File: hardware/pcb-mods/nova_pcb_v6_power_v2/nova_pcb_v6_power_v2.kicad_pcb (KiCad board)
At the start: 4 copper layers, 112 x 90 mm, 55 parts, among them J1 XT60_4S_IN, J12 XT30_JET_12V, J13 XT30_L2_12V, J2 UBEC_5V_AUX, J20 IB_2x06, J3 XT30_Inj, J4 XT30_Inj, J5 XT30_Inj, J6 XT30_Inj, J7 XT30_Inj, J8 ServoBus_TTL, M1 Voltmeter_DC, Q1 IRLB3034PBF, Q2 BSS138_cutoff, Q3 BSS138_estop, Q4 BSS138_jetcut, SW1 Rocker_30A, SW2 Estop_NC_latching, U1 Pololu_D42V110F7_LEG_7V5, U10 INA226, U11 INA226, U2 Pololu_D42V110F12_HIP_12V, U3 Pololu_D24V22F12_L2_12V, U4 Pololu_D42V55F12_JET_12V, U5 Pololu_D42V55F7_ARM_7V5, U8 LM393, U9 INA226

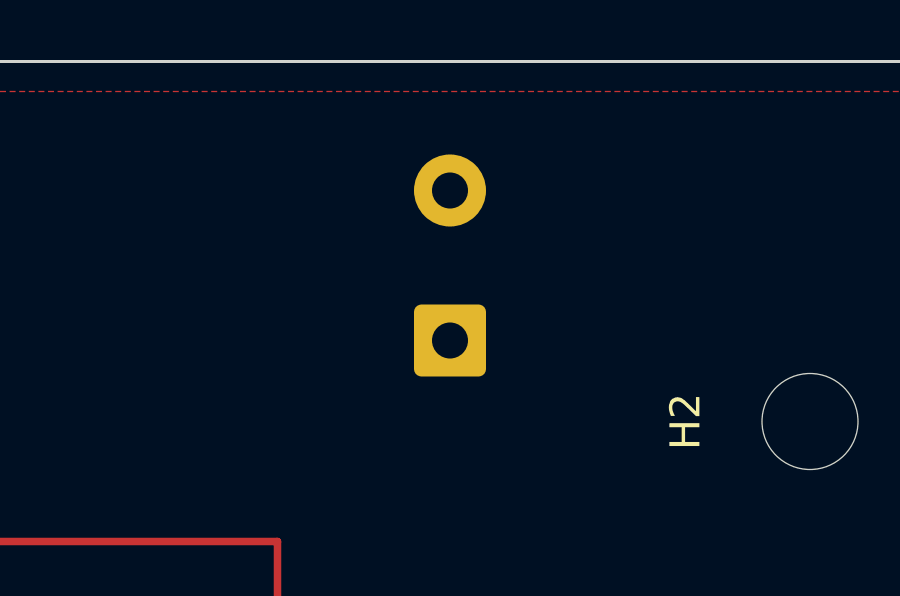
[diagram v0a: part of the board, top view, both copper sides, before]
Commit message: pcb(v6-power-v2): nudge C4 1.0mm inboard — edge clearance 0.3 -> 1.3mm
kicad-happy PM-002 error cleared. Pads feed LEG pour / GND plane only,
no tracks to move. Zones refilled, DRC 0 errors.

Co-Authored-By: Claude Fable 5 <noreply@anthropic.com>
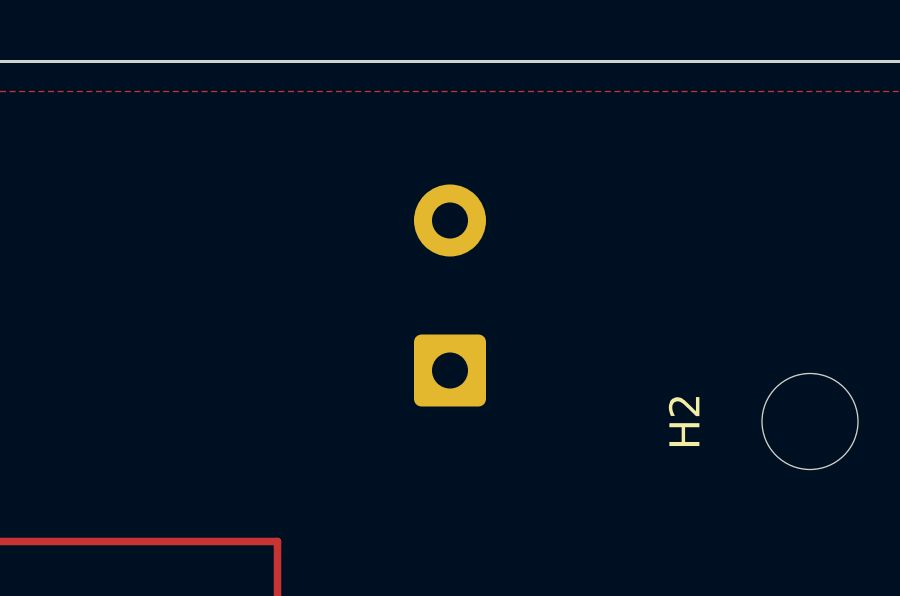
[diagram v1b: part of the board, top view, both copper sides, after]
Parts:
- moved C4 1.00 mm to (165.0, 61.3)
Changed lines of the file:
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@@
 	(footprint "Capacitor_THT:CP_Radial_D12.5mm_P5.00mm"
 		(layer "B.Cu")
-		(at 165 60.3 90)
+		(at 165 61.3 90)
 		(descr "CP, Radial series, Radial, pin pitch=5.00mm, diameter=12.5mm, height=20mm, Electrolytic Capacitor")
 		(tags "CP Radial series Radial pin pitch 5.00mm diameter 12.5mm height 20mm Electrolytic Capacitor")

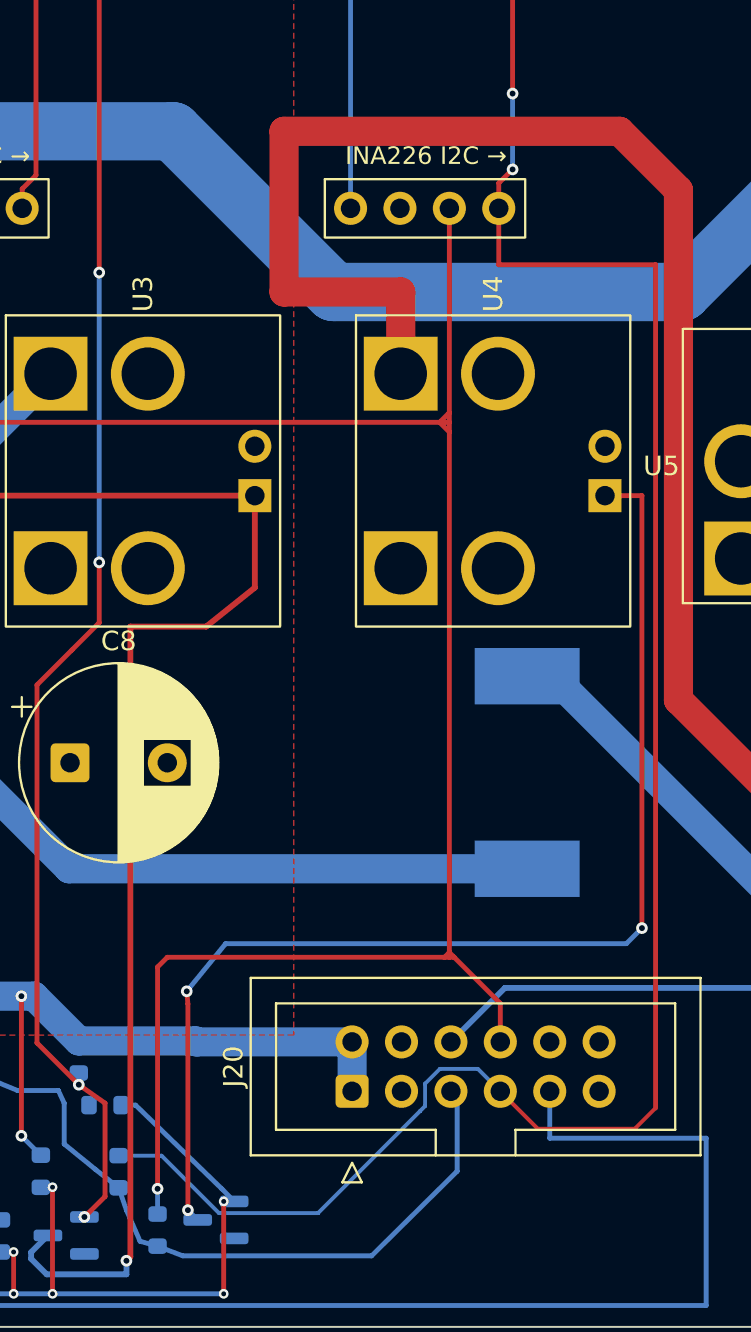
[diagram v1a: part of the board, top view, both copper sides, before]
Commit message: pcb(v6-power-v2): sync nova_v6 library footprints from board — 13->5 DRC mismatch warnings
INA226_Module_Breakout: 12-pad module -> 4-pad I2C header landing
(matches the off-board conversion; descr documents wiring + addresses).
Buck_Offboard_Terminal_2xXT30: synced board geometry to lib.
Remaining 5 warnings (J2 M1 Q1 SW1 SW2) = upstream KiCad 9 stock-lib
drift since placement — cosmetic, deliberately NOT updated pre-fab
(refreshing stock footprints can shift pads under routed copper).
Gerbers never consult libraries; zero fab impact.

Co-Authored-By: Claude Fable 5 <noreply@anthropic.com>
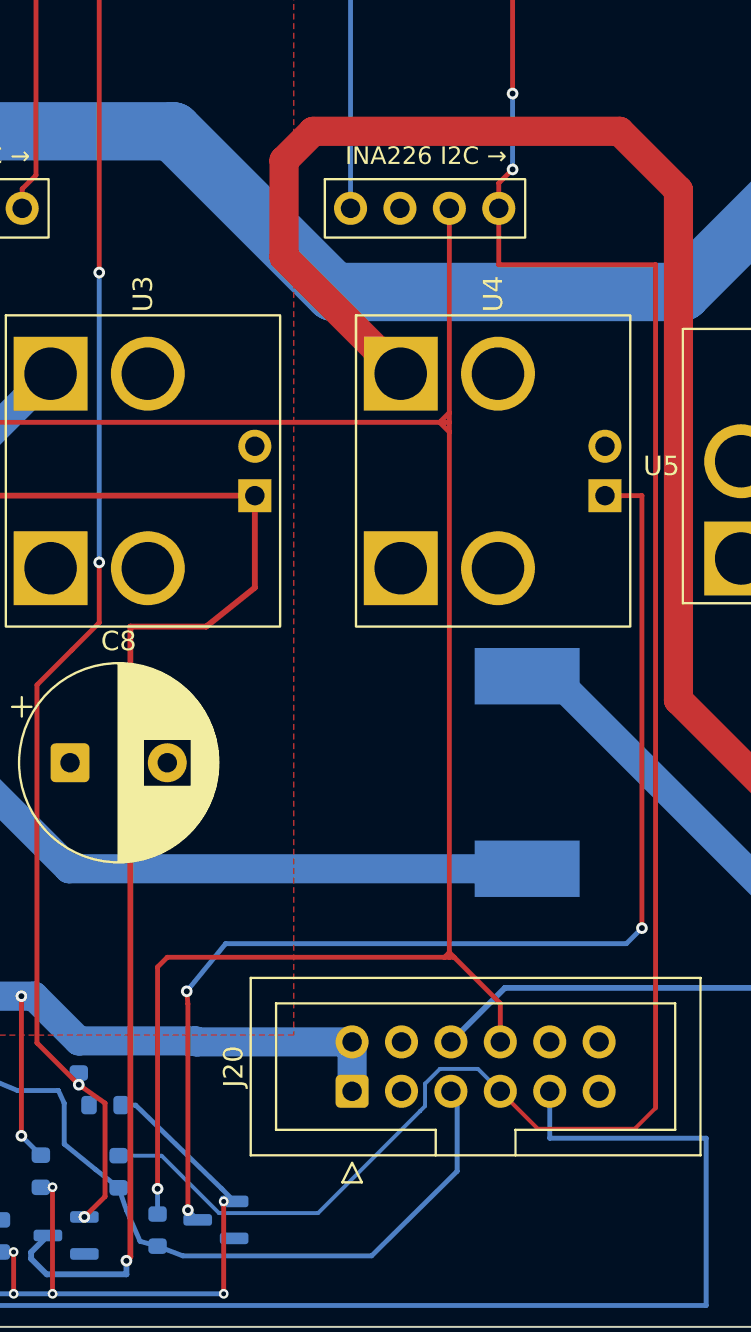
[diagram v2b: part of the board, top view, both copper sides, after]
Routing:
- net V12_JET: track 92.8 -> 88.4 mm
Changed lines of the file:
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@@
 			(pinfunction "Pin_4")
 			(pintype "passive")
+			(teardrops
+				(best_length_ratio 0.5)
+				(max_length 1)
+				(best_width_ratio 1)
+				(max_width 2)
+				(curved_edges no)
+				(filter_ratio 0.9)
+				(enabled yes)
+				(allow_two_segments yes)
+				(prefer_zone_connections yes)
+			)
 		)
 		(embedded_fonts no)
@@
 	)
 	(segment
-		(start 153.5 92)
-		(end 153.5 87.8)
+		(start 147.5 86)
+		(end 147.5 81.04)
 		(width 1.5)
 		(layer "F.Cu")
@@
 	)
 	(segment
-		(start 153.5 87.8)
-		(end 147.5 87.8)
+		(start 153.5 92)
+		(end 147.5 86)
 		(width 1.5)
 		(layer "F.Cu")
@@
 	)
 	(segment
-		(start 147.5 87.8)
-		(end 147.5 79.54)
+		(start 147.5 81.04)
+		(end 149 79.54)
 		(width 1.5)
 		(layer "F.Cu")
@@
 	)
 	(segment
-		(start 147.5 79.54)
+		(start 149 79.54)
 		(end 164.75 79.54)
 		(width 1.5)
@@
 	)
 	(segment
-		(start 111.25 81)
-		(end 110.54 81.8)
-		(width 0.25)
+		(start 139 132.2)
+		(end 141.208032 132.2)
+		(width 0.2)
 		(layer "B.Cu")
 		(net 13)
 	)
 	(segment
-		(start 149.2519 135.151)
-		(end 149.25 135.151)
+		(start 154.75 129.6529)
+		(end 154.75 128.5)
 		(width 0.2)
 		(layer "B.Cu")
@@
 	(segment
 		(start 155.511 127.739)
-		(end 154.75 128.5)
+		(end 157.469 127.739)
 		(width 0.2)
 		(layer "B.Cu")
@@
 	)
 	(segment
-		(start 154.75 128.5)
-		(end 154.75 129.6529)
-		(width 0.2)
+		(start 111.25 81)
+		(end 110.54 81.8)
+		(width 0.25)
 		(layer "B.Cu")
 		(net 13)
 	)
 	(segment
-		(start 158.62 128.89)
-		(end 157.469 127.739)
+		(start 141.208032 132.2)
+		(end 144.159032 135.151)
 		(width 0.2)
 		(layer "B.Cu")
@@
 	)
 	(segment
-		(start 149.25 135.151)
-		(end 144.159032 135.151)
+		(start 154.5 129.9029)
+		(end 154.75 129.6529)
 		(width 0.2)
 		(layer "B.Cu")
@@
 	)
 	(segment
-		(start 157.469 127.739)
-		(end 155.511 127.739)
+		(start 144.159032 135.151)
+		(end 149.25 135.151)
 		(width 0.2)
 		(layer "B.Cu")
@@
 	)
 	(segment
-		(start 154.75 129.6529)
-		(end 154.5 129.9029)
-		(width 0.2)
-		(layer "B.Cu")
-		(net 13)
-	)
-	(segment
-		(start 141.208032 132.2)
-		(end 139 132.2)
+		(start 149.25 135.151)
+		(end 154.4981 129.9029)
 		(width 0.2)
 		(layer "B.Cu")
@@
 	)
 	(segment
-		(start 154.4981 129.9029)
-		(end 149.25 135.151)
+		(start 157.469 127.739)
+		(end 158.62 128.89)
 		(width 0.2)
 		(layer "B.Cu")
@@
 	)
 	(segment
-		(start 144.159032 135.151)
-		(end 141.208032 132.2)
+		(start 154.75 128.5)
+		(end 155.511 127.739)
 		(width 0.2)
 		(layer "B.Cu")
@@
 	)
 	(segment
-		(start 154.5 129.9029)
-		(end 154.4981 129.9029)
+		(start 154.4981 129.9029)
+		(end 154.5 129.9029)
 		(width 0.2)
 		(layer "B.Cu")
@@
 		(name "$teardrop_padvia$")
 		(hatch none 0.1)
-		(priority 30000)
+		(priority 30001)
 		(attr
 			(teardrop
@@
 	)
 	(zone
-		(net 2)
-		(net_name "V7V5_LEG")
+		(net 12)
+		(net_name "I2C_SCL")
 		(layer "F.Cu")
-		(hatch edge 0.5)
-		(priority 2)
-		(connect_pads
-			(clearance 0.5)
+		(name "$teardrop_padvia$")
+		(hatch none 0.1)
+		(priority 30002)
+		(attr
+			(teardrop
+				(type padvia)
+			)
 		)
-		(min_thickness 0.4)
+		(connect_pads yes
+			(clearance 0)
+		)
+		(min_thickness 0.0254)
 		(filled_areas_thickness no)
 		(fill yes
 			(thermal_gap 0.5)
 			(thermal_bridge_width 0.5)
+			(island_removal_mode 1)
+			(island_area_min 10)
 		)
 		(polygon
 			(pts
-				(xy 86 67) (xy 142 67) (xy 142 52) (xy 196 52) (xy 196 72.5) (xy 148 72.5) (xy 148 126) (xy 86 126)
+				(xy 158.745 124.666333) (xy 158.495 124.666333) (xy 157.913251 125.877765) (xy 158.62 126.351) (xy 159.326749 125.877765)
 			)
 		)
@@
 		(name "$teardrop_padvia$")
 		(hatch none 0.1)
-		(priority 30003)
+		(priority 30004)
 		(attr
 			(teardrop
@@
 	)
 	(zone
+		(net 2)
+		(net_name "V7V5_LEG")
+		(layer "F.Cu")
+		(hatch edge 0.5)
+		(priority 2)
+		(connect_pads
+			(clearance 0.5)
+		)
+		(min_thickness 0.4)
+		(filled_areas_thickness no)
+		(fill yes
+			(thermal_gap 0.5)
+			(thermal_bridge_width 0.5)
+		)
+		(polygon
+			(pts
+				(xy 86 67) (xy 142 67) (xy 142 52) (xy 196 52) (xy 196 72.5) (xy 148 72.5) (xy 148 126) (xy 86 126)
+			)
+		)
+	)
+	(zone
 		(net 12)
 		(net_name "I2C_SCL")
@@
 		(name "$teardrop_padvia$")
 		(hatch none 0.1)
-		(priority 30002)
+		(priority 30003)
 		(attr
 			(teardrop
@@
 	)
 	(zone
-		(net 12)
-		(net_name "I2C_SCL")
+		(net 10)
+		(net_name "V12_JET")
 		(layer "F.Cu")
 		(name "$teardrop_padvia$")
 		(hatch none 0.1)
-		(priority 30001)
+		(priority 30000)
 		(attr
 			(teardrop
@@
 		(polygon
 			(pts
-				(xy 158.745 124.666333) (xy 158.495 124.666333) (xy 157.913251 125.877765) (xy 158.62 126.351) (xy 159.326749 125.877765)
+				(xy 151.423224 88.862564) (xy 150.362564 89.923224) (xy 151.6 91.514213) (xy 153.500707 92.000707)
+				(xy 153.014213 90.1)
 			)
 		)
 	)
 	(zone
-		(net 8)
-		(net_name "V5_AUX")
+		(net 14)
+		(net_name "BATT_LOW")
 		(layer "B.Cu")
 		(name "$teardrop_padvia$")
 		(hatch none 0.1)
-		(priority 30002)
+		(priority 30005)
 		(attr
 			(teardrop
@@
 		(polygon
 			(pts
-				(xy 151.75 127.19) (xy 150.25 127.19) (xy 150.15 128.29) (xy 151 128.891) (xy 151.85 128.29)
+				(xy 161.035 130.573667) (xy 161.285 130.573667) (xy 161.866749 129.362235) (xy 161.16 128.889) (xy 160.453251 129.362235)
 			)
 		)
 	)
 	(zone
-		(net 17)
-		(net_name "EN_BUCKS")
+		(net 9)
+		(net_name "BUS_SERVO")
 		(layer "B.Cu")
 		(name "$teardrop_padvia$")
 		(hatch none 0.1)
-		(priority 30007)
+		(priority 30004)
 		(attr
 			(teardrop
@@
 		(polygon
 			(pts
-				(xy 134.744302 136.706066) (xy 134.956434 136.918198) (xy 135.486764 136.6) (xy 135.363207 136.299293)
-				(xy 134.676868 136.561367)
+				(xy 189.334227 96.615405) (xy 189.546359 96.827537) (xy 190.875 96.85) (xy 191.000707 95.999293)
+				(xy 190.168251 95.527765)
 			)
 		)
@@
 		(name "$teardrop_padvia$")
 		(hatch none 0.1)
-		(priority 30001)
+		(priority 30002)
 		(attr
 			(teardrop
@@
 		(polygon
 			(pts
-				(xy 149.316333 125.6) (xy 149.316333 127.1) (xy 150.834173 127.183667) (xy 151.001 126.35) (xy 150.834173 125.516333)
+				(xy 151.75 127.19) (xy 150.25 127.19) (xy 150.15 128.29) (xy 151 128.891) (xy 151.85 128.29)
 			)
 		)
 	)
 	(zone
-		(net 14)
-		(net_name "BATT_LOW")
+		(net 17)
+		(net_name "EN_BUCKS")
 		(layer "B.Cu")
 		(name "$teardrop_padvia$")
 		(hatch none 0.1)
-		(priority 30005)
+		(priority 30007)
 		(attr
 			(teardrop
@@
 		(polygon
 			(pts
-				(xy 161.035 130.573667) (xy 161.285 130.573667) (xy 161.866749 129.362235) (xy 161.16 128.889) (xy 160.453251 129.362235)
+				(xy 134.744302 136.706066) (xy 134.956434 136.918198) (xy 135.486764 136.6) (xy 135.363207 136.299293)
+				(xy 134.676868 136.561367)
 			)
 		)
 	)
 	(zone
-		(net 11)
-		(net_name "+3V3")
+		(net 13)
+		(net_name "I2C_SDA")
 		(layer "B.Cu")
 		(name "$teardrop_padvia$")
 		(hatch none 0.1)
-		(priority 30003)
+		(priority 30006)
 		(attr
 			(teardrop
@@
 		(polygon
 			(pts
-				(xy 156.275 130.509807) (xy 156.525 130.509807) (xy 156.913667 129.055827) (xy 156.08 128.889) (xy 155.373251 129.362235)
+				(xy 157.413092 127.639) (xy 157.413092 127.839) (xy 157.786333 129.055827) (xy 158.621 128.89) (xy 158.785827 128.056333)
 			)
 		)
 	)
 	(zone
-		(net 9)
-		(net_name "BUS_SERVO")
+		(net 8)
+		(net_name "V5_AUX")
 		(layer "B.Cu")
 		(name "$teardrop_padvia$")
 		(hatch none 0.1)
-		(priority 30004)
+		(priority 30000)
 		(attr
 			(teardrop
@@
 		(polygon
 			(pts
-				(xy 189.334227 96.615405) (xy 189.546359 96.827537) (xy 190.875 96.85) (xy 191.000707 95.999293)
-				(xy 190.168251 95.527765)
+				(xy 150.25 128.033667) (xy 151.75 128.033667) (xy 151.833667 126.515827) (xy 151 126.349) (xy 150.166333 126.515827)
 			)
 		)
@@
 	)
 	(zone
-		(net 13)
-		(net_name "I2C_SDA")
+		(net 8)
+		(net_name "V5_AUX")
 		(layer "B.Cu")
 		(name "$teardrop_padvia$")
 		(hatch none 0.1)
-		(priority 30006)
+		(priority 30001)
 		(attr
 			(teardrop
@@
 		(polygon
 			(pts
-				(xy 157.413092 127.639) (xy 157.413092 127.839) (xy 157.786333 129.055827) (xy 158.621 128.89) (xy 158.785827 128.056333)
+				(xy 149.316333 125.6) (xy 149.316333 127.1) (xy 150.834173 127.183667) (xy 151.001 126.35) (xy 150.834173 125.516333)
 			)
 		)
 	)
 	(zone
-		(net 8)
-		(net_name "V5_AUX")
+		(net 11)
+		(net_name "+3V3")
 		(layer "B.Cu")
 		(name "$teardrop_padvia$")
 		(hatch none 0.1)
-		(priority 30000)
+		(priority 30003)
 		(attr
 			(teardrop
@@
 		(polygon
 			(pts
-				(xy 150.25 128.033667) (xy 151.75 128.033667) (xy 151.833667 126.515827) (xy 151 126.349) (xy 150.166333 126.515827)
+				(xy 156.275 130.509807) (xy 156.525 130.509807) (xy 156.913667 129.055827) (xy 156.08 128.889) (xy 155.373251 129.362235)
 			)
 		)

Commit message: pcb(v6-power-v2): BOARD COMPLETE — pour seams closed, GND orphans stitched, DRC 0/0
- LEG pour islands bridged: 2.5mm F.Cu trunk crossing y67 west of the
  SDA fence (x109), no vias in the 9A path
- GND orphan islands stitched to In1 plane: Q4 source + R16 pulldown
  (both were FLOATING — Jetson cutoff + gate-default-off would have
  shipped dead) + comb fragments; inter-pad slivers culled at 8mm²
- DRC: 0 errors, 0 unconnected. Remaining warnings cosmetic only
  (5 stock-lib drift, 1 silk-over-copper).

Co-Authored-By: Claude Fable 5 <noreply@anthropic.com>
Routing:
- net V7V5_LEG: track 38.4 -> 78.9 mm
- net GND: vias 0 -> 4
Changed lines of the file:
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@@
 		)
+	)
+	(via
+		(at 158.369045 130.410004)
+		(size 0.6)
+		(drill 0.3)
+		(layers "F.Cu" "B.Cu")
+		(net 1)
+	)
+	(via
+		(at 146.5 136.3)
+		(size 0.6)
+		(drill 0.3)
+		(layers "F.Cu" "B.Cu")
+		(net 1)
+	)
+	(via
+		(at 141.818486 133.780115)
+		(size 0.6)
+		(drill 0.3)
+		(layers "F.Cu" "B.Cu")
+		(net 1)
+	)
+	(via
+		(at 138.3 127.7)
+		(size 0.6)
+		(drill 0.3)
+		(layers "F.Cu" "B.Cu")
+		(net 1)
+	)
+	(segment
+		(start 109 64.599999)
+		(end 110.1 63.5)
+		(width 2.5)
+		(layer "F.Cu")
+		(net 2)
 	)
 	(segment
@@
 	)
 	(segment
+		(start 110.1 63.5)
+		(end 146 63.5)
+		(width 2.5)
+		(layer "F.Cu")
+		(net 2)
+	)
+	(segment
 		(start 186.25 73.75)
 		(end 191 69)
@@
 		(end 191 98.5)
 		(width 2)
+		(layer "F.Cu")
+		(net 2)
+	)
+	(segment
+		(start 109 67.7)
+		(end 109 64.599999)
+		(width 2.5)
 		(layer "F.Cu")
 		(net 2)
@@
 			(thermal_gap 0.3)
 			(thermal_bridge_width 0.5)
+			(island_removal_mode 2)
+			(island_area_min 8)
 		)
 		(polygon
